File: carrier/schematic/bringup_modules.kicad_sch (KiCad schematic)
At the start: 56 parts, among them U301 SY6280AAC, U302 SY6280AAC, U303 SY6280AAC, U304 SY6280AAC, U305 SY6280AAC, U306 SY6280AAC, U307 SY6280AAC, U308 SY6280AAC

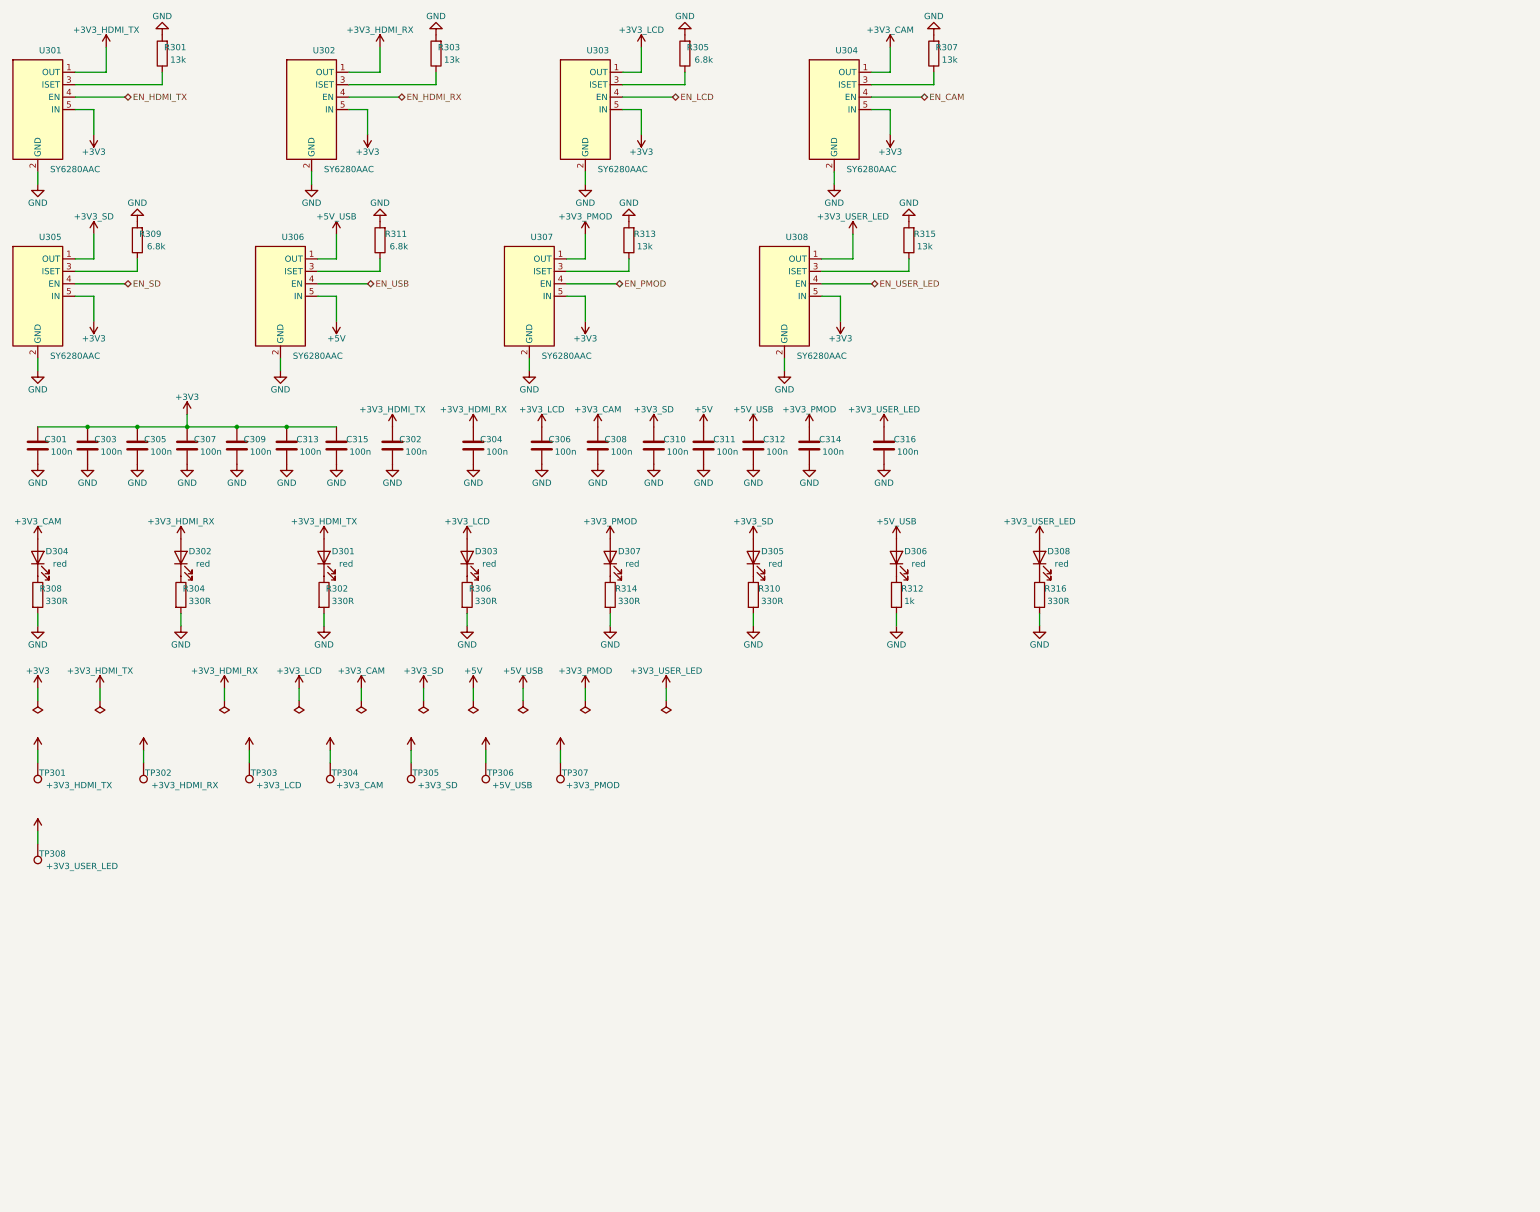
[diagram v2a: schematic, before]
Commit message: bringup: 5V MODULE GATES (PLAN round 5) — +5V_HDMI_TX/+5V_LCD SY6280 cells
Two new module gate cells resolve the power tree's last two UNSOURCED
findings, following the existing per-module pattern exactly:
- bringup_modules U9 +5V -> +5V_HDMI_TX (RSET 13k = 523 mA backstop; the
  load is TPD12S016-internally limited to 55 mA, DS 7.3.10) and U10
  +5V -> +5V_LCD (RSET 6.8k = 1.0 A for the 450 mA boost budget), 100n
  in/out, 1k status LEDs, TPs at the gated source.
- bringup_en_modules: 2 new SN74LVC1G08 AND cells (DIP master, SW veto).
- bringup_rails: SW1/SW2 positions were EXHAUSTED -> honest extension DIP
  SW6 (DSHP04TSGER, already-verified part; pos 1/2 wired, 3/4 author-NC
  spares) + TCA9535 P12/P13 vetos (P11 stays reserved for PMON_ALERT_N).
- bringup_facts.dip_switch_refs(): manual/firmware generators now discover
  every DSHP DIP instead of hard-coding SW1/SW2 — BRINGUP.md + the SC
  contract header regenerated with the new EN map automatically
  (ZC_TCA9535_BIT_EN_HDMI_TX_5V=10 / _EN_LCD_5V=11, SW6 stage-4 rows).
POWER TREE PASS: 14 regulators, findings 4->2, +5V buck at 91 % of 3 A.
All gates green (board exit 0); 3 drifted renders eyeballed full-res and
blessed; PWR_FLAG policy auto-stripped the now-driven rails' flags.

Co-Authored-By: Claude Fable 5 <noreply@anthropic.com>
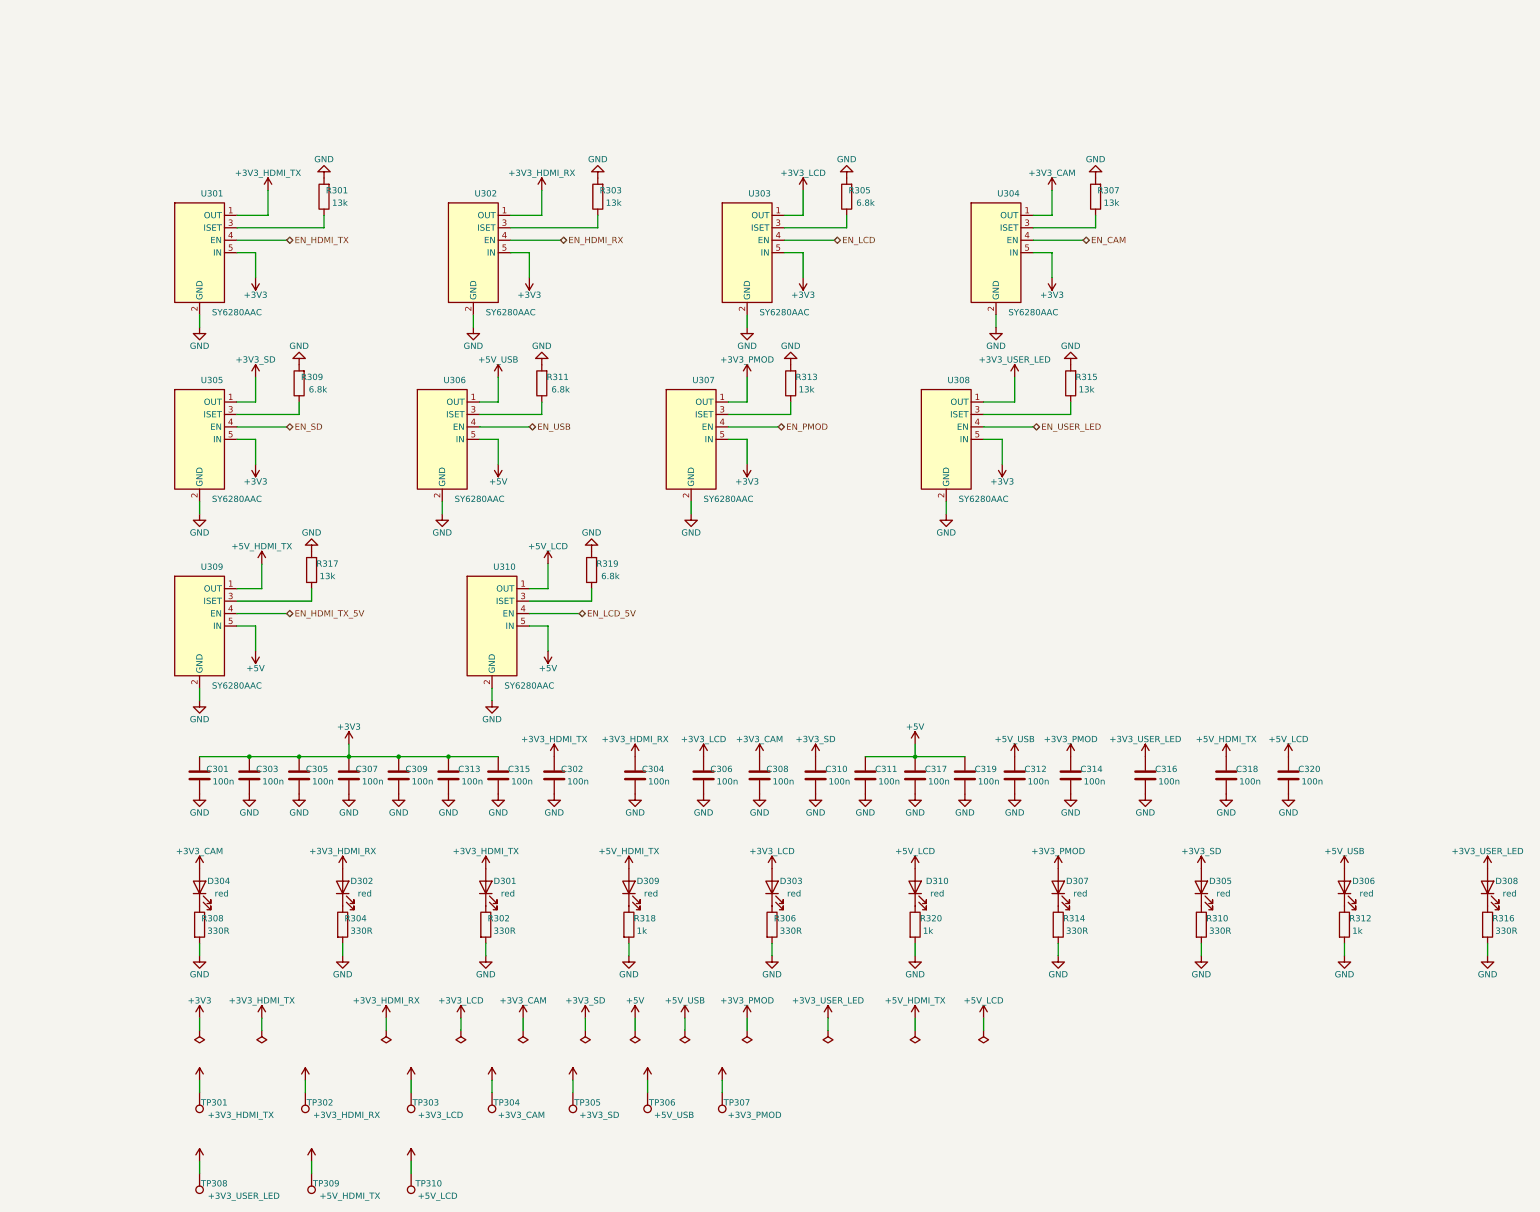
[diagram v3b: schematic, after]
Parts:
- added D306, D308: red, LED_SMD:LED_0603_1608Metric, symbol Device:LED
- added R312: 1k, Resistor_SMD:R_0603_1608Metric, symbol Device:R
- added R316: 330R, Resistor_SMD:R_0603_1608Metric, symbol Device:R
- added TP301: +3V3_HDMI_TX, TestPoint:TestPoint_Pad_D1.5mm, symbol Connector:TestPoint
- added TP302: +3V3_HDMI_RX, TestPoint:TestPoint_Pad_D1.5mm, symbol Connector:TestPoint
- added TP303: +3V3_LCD, TestPoint:TestPoint_Pad_D1.5mm, symbol Connector:TestPoint
- added TP304: +3V3_CAM, TestPoint:TestPoint_Pad_D1.5mm, symbol Connector:TestPoint
- added TP305: +3V3_SD, TestPoint:TestPoint_Pad_D1.5mm, symbol Connector:TestPoint
- added TP306: +5V_USB, TestPoint:TestPoint_Pad_D1.5mm, symbol Connector:TestPoint
- added TP307: +3V3_PMOD, TestPoint:TestPoint_Pad_D1.5mm, symbol Connector:TestPoint
- added TP308: +3V3_USER_LED, TestPoint:TestPoint_Pad_D1.5mm, symbol Connector:TestPoint
- added TP309: +5V_HDMI_TX, TestPoint:TestPoint_Pad_D1.5mm, symbol Connector:TestPoint
- added TP310: +5V_LCD, TestPoint:TestPoint_Pad_D1.5mm, symbol Connector:TestPoint
- C311: renamed from D304; value red -> 100n; footprint LED_SMD:LED_0603_1608Metric -> Capacitor_SMD:C_0603_1608Metric; symbol Device:LED -> Device:C; LCSC C2286 -> C1591
- C312: renamed from R304; value 330R -> 100n; footprint Resistor_SMD:R_0603_1608Metric -> Capacitor_SMD:C_0603_1608Metric; symbol Device:R -> Device:C; LCSC C23138 -> C1591
- C314: renamed from D301; value red -> 100n; footprint LED_SMD:LED_0603_1608Metric -> Capacitor_SMD:C_0603_1608Metric; symbol Device:LED -> Device:C; LCSC C2286 -> C1591
- C316: renamed from R302; value 330R -> 100n; footprint Resistor_SMD:R_0603_1608Metric -> Capacitor_SMD:C_0603_1608Metric; symbol Device:R -> Device:C; LCSC C23138 -> C1591
- C317: renamed from R308; value 330R -> 100n; footprint Resistor_SMD:R_0603_1608Metric -> Capacitor_SMD:C_0603_1608Metric; symbol Device:R -> Device:C; LCSC C23138 -> C1591
- C318: renamed from D303; value red -> 100n; footprint LED_SMD:LED_0603_1608Metric -> Capacitor_SMD:C_0603_1608Metric; symbol Device:LED -> Device:C; LCSC C2286 -> C1591
- C319: renamed from D302; value red -> 100n; footprint LED_SMD:LED_0603_1608Metric -> Capacitor_SMD:C_0603_1608Metric; symbol Device:LED -> Device:C; LCSC C2286 -> C1591
- C320: renamed from R306; value 330R -> 100n; footprint Resistor_SMD:R_0603_1608Metric -> Capacitor_SMD:C_0603_1608Metric; symbol Device:R -> Device:C; LCSC C23138 -> C1591
- D303: renamed from TP301; value +3V3_HDMI_TX -> red; footprint TestPoint:TestPoint_Pad_D1.5mm -> LED_SMD:LED_0603_1608Metric; symbol Connector:TestPoint -> Device:LED; BOM exclude -> (none); LCSC (none) -> C2286
- D305: renamed from TP307; value +3V3_PMOD -> red; footprint TestPoint:TestPoint_Pad_D1.5mm -> LED_SMD:LED_0603_1608Metric; symbol Connector:TestPoint -> Device:LED; BOM exclude -> (none); LCSC (none) -> C2286
- D307: renamed from TP305; value +3V3_SD -> red; footprint TestPoint:TestPoint_Pad_D1.5mm -> LED_SMD:LED_0603_1608Metric; symbol Connector:TestPoint -> Device:LED; BOM exclude -> (none); LCSC (none) -> C2286
- D310: renamed from TP303; value +3V3_LCD -> red; footprint TestPoint:TestPoint_Pad_D1.5mm -> LED_SMD:LED_0603_1608Metric; symbol Connector:TestPoint -> Device:LED; BOM exclude -> (none); LCSC (none) -> C2286
- R302: renamed from R312; value 1k -> 330R; LCSC C21190 -> C23138
- R306: renamed from TP302; value +3V3_HDMI_RX -> 330R; footprint TestPoint:TestPoint_Pad_D1.5mm -> Resistor_SMD:R_0603_1608Metric; symbol Connector:TestPoint -> Device:R; BOM exclude -> (none); LCSC (none) -> C23138
- R310: renamed from TP308; value +3V3_USER_LED -> 330R; footprint TestPoint:TestPoint_Pad_D1.5mm -> Resistor_SMD:R_0603_1608Metric; symbol Connector:TestPoint -> Device:R; BOM exclude -> (none); LCSC (none) -> C23138
- R314: renamed from TP306; value +5V_USB -> 330R; footprint TestPoint:TestPoint_Pad_D1.5mm -> Resistor_SMD:R_0603_1608Metric; symbol Connector:TestPoint -> Device:R; BOM exclude -> (none); LCSC (none) -> C23138
- R317: renamed from C303; value 100n -> 13k; footprint Capacitor_SMD:C_0603_1608Metric -> Resistor_SMD:R_0603_1608Metric; symbol Device:C -> Device:R; LCSC C1591 -> C22797
- R318: renamed from R316; value 330R -> 1k; LCSC C23138 -> C21190
- R319: renamed from C307; value 100n -> 6.8k; footprint Capacitor_SMD:C_0603_1608Metric -> Resistor_SMD:R_0603_1608Metric; symbol Device:C -> Device:R; LCSC C1591 -> C23212
- R320: renamed from TP304; value +3V3_CAM -> 1k; footprint TestPoint:TestPoint_Pad_D1.5mm -> Resistor_SMD:R_0603_1608Metric; symbol Connector:TestPoint -> Device:R; BOM exclude -> (none); LCSC (none) -> C21190
- U309: renamed from C301; value 100n -> SY6280AAC; footprint Capacitor_SMD:C_0603_1608Metric -> SY6280AAC:SY6280AAC; symbol Device:C -> SY6280AAC:SY6280AAC; LCSC C1591 -> C55136
- U310: renamed from C305; value 100n -> SY6280AAC; footprint Capacitor_SMD:C_0603_1608Metric -> SY6280AAC:SY6280AAC; symbol Device:C -> SY6280AAC:SY6280AAC; LCSC C1591 -> C55136
- renumbered C309 to C301, C310 to C302, C313 to C303, C311 to C304, C315 to C305, C312 to C306, C302 to C307, C314 to C308, C304 to C309, C316 to C310, C306 to C313, C308 to C315, D306 to D301, D305 to D302, D307 to D304, D308 to D309, R310 to R304, R314 to R308
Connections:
- net +3V3: now also C307.1, C309.1, C313.1, C315.1; no longer R317.1, R319.1, U309.1, U310.1
- net +3V3_CAM: now also C308.1, D304.2 (A), TP304.1; no longer C311.2 (A), C315.1, R320.1
- net +3V3_HDMI_RX: now also C304.1, D302.2 (A), TP302.1; no longer C309.1, C319.2 (A), R306.1
- net +3V3_HDMI_TX: now also C302.1, D301.2 (A), TP301.1; no longer C307.1, C314.2 (A), D303.1
- net +3V3_LCD: now also C306.1, D303.2 (A), TP303.1; no longer C313.1, C318.2 (A), D310.1
- net +3V3_PMOD: now also C314.1, D307.2 (A), TP307.1; no longer C308.1, D304.2 (A), D305.1
- net +3V3_SD: now also C310.1, D305.2 (A), TP305.1; no longer C302.1, D302.2 (A), D307.1
- net +3V3_USER_LED: now also C316.1, D308.2 (A), TP308.1; no longer C310.1, D309.2 (A), R310.1
- net +5V: now also C311.1, C317.1, C319.1, U309.5 (IN), U310.5 (IN); no longer C304.1
- net +5V_USB: now also C312.1, D306.2 (A), TP306.1; no longer C306.1, D301.2 (A), R314.1
- net GND: now also C311.2, C314.2, C318.2, C319.2, R306.2, R310.2, R314.2, R320.2, R312.2, R316.2
- net +5V_HDMI_TX: now reaches C318.1
- net +5V_HDMI_TX: now also D309.2 (A), U309.1 (OUT), TP309.1; no longer C320.1
- new net: R317.1, U309.3 (ISET)
- new net: D305.1 (K), R310.1
- new net: D306.1 (K), R312.1
- new net: D303.1 (K), R306.1
- new net: D310.1 (K), R320.1
- new net: D308.1 (K), R316.1
- new net: D307.1 (K), R314.1
- new net: R319.1, U310.3 (ISET)
- new net +5V_LCD: C320.1, D310.2 (A), TP310.1, U310.1 (OUT)
- new net EN_HDMI_TX_5V: U309.4 (EN)
- new net EN_LCD_5V: U310.4 (EN)
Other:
- moved on the sheet: C301, C302, C303, C304, C305, C306, C307, C308, C309, C310, C313, C315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

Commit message: audit-fix(engine): harvest F1-F7,F9 — gate hardening + leak + guards
F1 selftest now exercises the VISUAL gate against geometry mutants (wire-cross
+ text-over-wire) — proven to bite (was never run on a mutant before).
F2 visual_gate catches different-net wire T-touch / butt-join shorts.
F3 netlist_gate no longer leaks tmp .net files (was 2671 stale).
F4 board uniquify guards the stride (widened 100->1000) against ref collision.
F5 hier-mode sheets now re-run through the per-sheet netlist gate.
F6 dead clause dropped; F7 stale zynq_eda docstring fixed; F9 eager inline-pin
validation. Source copied verbatim from the audit-fix worktree (6 files, proven
untouched on origin since its base); board regenerated fresh. All gates green,
selftest geo-mutants killed by the visual gate, goldens 23/23, m1_rc PASS.

Co-Authored-By: Claude Fable 5 <noreply@anthropic.com>
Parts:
- renumbered C301 to C3001, C302 to C3002, C303 to C3003, C304 to C3004, C305 to C3005, C306 to C3006, C307 to C3007, C308 to C3008, C309 to C3009, C310 to C3010, C311 to C3011, C312 to C3012, C313 to C3013, C314 to C3014, C315 to C3015, C316 to C3016, C317 to C3017, C318 to C3018, C319 to C3019, C320 to C3020, D301 to D3001, D302 to D3002, D303 to D3003, D304 to D3004, D305 to D3005, D306 to D3006, D307 to D3007, D308 to D3008, D309 to D3009, D310 to D3010, R301 to R3001, R302 to R3002, R303 to R3003, R304 to R3004, R305 to R3005, R306 to R3006, R307 to R3007, R308 to R3008, R309 to R3009, R310 to R3010, R311 to R3011, R312 to R3012, R313 to R3013, R314 to R3014, R315 to R3015, R316 to R3016, R317 to R3017, R318 to R3018, R319 to R3019, R320 to R3020, TP301 to TP3001, TP302 to TP3002, TP303 to TP3003, TP304 to TP3004, TP305 to TP3005, TP306 to TP3006, TP307 to TP3007, TP308 to TP3008, TP309 to TP3009, TP310 to TP3010, U301 to U3001, U302 to U3002, U303 to U3003, U304 to U3004, U305 to U3005, U306 to U3006, U307 to U3007, U308 to U3008, U309 to U3009, U310 to U3010

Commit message: genpolish: TITLE-1 — populate the schematic title block on every sheet
Every sheet rendered a blank Title/Rev/Date — the clearest 'not a real
schematic' tell. emit() now writes a (title_block ...) after the paper node:
title = the sheet circuit's title, company "Zynq SoM Carrier", and a
"<sheet> — generated by schgen (do not hand-edit)" comment. NO date node — a
wall-clock date would break byte-determinism; the content-derived fields keep
every rebuild identical. Verified on A4 (usb_pd) and the dense A3 (power): the
block fills the standard reserved corner with zero drawing overlap. All 26
sheets, goldens re-blessed, board PASS + deterministic, selftest 53/53, m1,
pytest 147.

Co-Authored-By: Claude Opus 4.8 <noreply@anthropic.com>
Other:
- company: (none) -> Zynq SoM Carrier
- title: (none) -> Bring-up module gates: 10x SY6280 + status/user LEDs
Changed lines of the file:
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@@
 	(generator_version "1.0")
 	(paper "A3")
+	(title_block
+		(title "Bring-up module gates: 10x SY6280 + status/user LEDs")
+		(company "Zynq SoM Carrier")
+		(comment 1 "bringup_modules — generated by schgen (do not hand-edit)")
+	)
 	(wire
 		(pts

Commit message: board: four board-management HW blocks on a manually-gated +3V3_AUX (BOARDHW)
The four services the carrier was missing — all behind ONE manual power enable
(C1) on two new sheets split so neither defeats the placer's rail-stub router:

  board_aux       — the gate + I2C isolator (infrastructure)
  board_services  — ID-EEPROM + RTC + watchdog + QWIIC (the peripherals)

WHAT LANDED
  * 24AA025E48 (C129895)  ID-EEPROM with a factory EUI-48 **MAC** for the
      LAN8720/RJ45 — strapped 0x51 (0x50 is the FMC EEPROM).
  * RV-3028-C7 (C3019759) I2C RTC, integrated DTCXO (no crystal), CR1220 coin
      cell (KH-CR1220-2) with auto-switchover, 0x52.
  * TPS3823-33 (C7719)    supervisor + windowed watchdog.
  * ZX-SH1.0-4PWT (C7430446)  QWIIC / STEMMA-QT expansion (gated 3V3 + the
      isolated AUX I2C).
  * SY6280 gate + DSHP04 DIP + PCA9306 isolator complete the infrastructure.

CONSTRAINTS (the user's three standing requirements)
  C1 manual enable "like the previous": +3V3_AUX is a SY6280 load switch whose
     EN is a default-OFF DSHP04 DIP (100k pulldown) — the same gated-module
     idiom, self-contained so it touches none of the dense rail/EN sheets.
  C2 "no watchdog reset during power-up": THREE independent guards — (1) the
     supervisor's VDD is the default-OFF +3V3_AUX, so it is UNPOWERED through
     power-up; (2) the TPS3823 disables its watchdog while WDI floats, and WDI
     is driven only by the PL (WATCHDOG_KICK, Hi-Z until the fabric is up); (3)
     RESET# is a firmware-mediated PL EVENT (J3.31), never a rail/POR line.
  C3 Zynq-agnostic: the only SoM-side signals (the 2 watchdog lines) ride PL
     bank-35 IO by their contract net names (IO_L16_N/P_35 -> J3.29/31); xdc.py
     emits the constraints live — nothing hard-codes the Zynq part.

LAW 0 (electrical integrity): the peripherals sit on the GATED rail but their
bus is the always-on STM32_I2C2 management bus. A PCA9306 bridges them with EN
tied to +3V3_AUX, so the switch OPENS whenever the rail is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
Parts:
- renumbered C3001 to C5001, C3002 to C5002, C3003 to C5003, C3004 to C5004, C3005 to C5005, C3006 to C5006, C3007 to C5007, C3008 to C5008, C3009 to C5009, C3010 to C5010, C3011 to C5011, C3012 to C5012, C3013 to C5013, C3014 to C5014, C3015 to C5015, C3016 to C5016, C3017 to C5017, C3018 to C5018, C3019 to C5019, C3020 to C5020, D3001 to D5001, D3002 to D5002, D3003 to D5003, D3004 to D5004, D3005 to D5005, D3006 to D5006, D3007 to D5007, D3008 to D5008, D3009 to D5009, D3010 to D5010, R3001 to R5001, R3002 to R5002, R3003 to R5003, R3004 to R5004, R3005 to R5005, R3006 to R5006, R3007 to R5007, R3008 to R5008, R3009 to R5009, R3010 to R5010, R3011 to R5011, R3012 to R5012, R3013 to R5013, R3014 to R5014, R3015 to R5015, R3016 to R5016, R3017 to R5017, R3018 to R5018, R3019 to R5019, R3020 to R5020, TP3001 to TP5001, TP3002 to TP5002, TP3003 to TP5003, TP3004 to TP5004, TP3005 to TP5005, TP3006 to TP5006, TP3007 to TP5007, TP3008 to TP5008, TP3009 to TP5009, TP3010 to TP5010, U3001 to U5001, U3002 to U5002, U3003 to U5003, U3004 to U5004, U3005 to U5005, U3006 to U5006, U3007 to U5007, U3008 to U5008, U3009 to U5009, U3010 to U5010

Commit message: audit fixes: QWIIC ESD on its own sheet + firmware I2C-map completeness
Acting on a multi-agent adversarial re-audit of the 28-sheet board. Each
finding was independently re-verified before action — two confident "HIGH"
findings were FALSE POSITIVES whose proposed fixes would have INTRODUCED bugs,
and are documented-rejected, not applied:

  * "DSHP04 switches in parallel" — wrong. The footprint pads prove the pairing
    by physical opposition (switch n = pads n & 9-n): switch 1 = pads 1&8 is the
    only one on EN_AUX; the other even pins (2/4/6) are NC, identical to the
    proven bringup_rails SW6 idiom. The proposed "fix" (pins 1+2) wires two
    DIFFERENT switches and would leave EN_AUX permanently pulled down — the rail
    could never enable.
  * "PCA9306 EN floats when AUX is off" — wrong. A 100k to a 0 V rail pulls EN
    to 0 V (disabled), which is exactly TI's recommended "isolate when the gated
    side is unpowered" connection. No float.

REAL findings actioned:

1. QWIIC connector lacked ESD (every other external connector has it). Moved the
   QWIIC out of board_services onto its own sheet board_qwiic (the carrier's
   connectors-get-their-own-sheet idiom — rj45_connector, usb_uart_connector)
   and added a USBLC6-2SC6 low-cap ESD array at the connector (1<->6 / 3<->4
   passthrough, clamp ref +3V3_AUX). The dedicated sheet also keeps both sheets
   sparse enough for the rail-stub router. board_services drops to 9 parts.

2. schgen/firmware.py loaded only 7 sheets, so the SC-firmware contract + its
   I2C address-collision check were BLIND to the new devices. Added board_aux/
   board_services to SOURCES and three address rows: FMC-EEPROM 0x50, ID-EEPROM
   0x51 (DERIVED from the 24AA025E48 A1/A0 straps, so a mis-strap to 0x50 now
   trips the collision check against the FMC EEPROM), RTC 0x52. The firmware can
   now address the EUI-48 MAC EEPROM and the RTC. 114 -> 117 #defines.

3. board_services docstring clarified (EEPROM/RTC are on the PCA9306-i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
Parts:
- renumbered C5001 to C6001, C5002 to C6002, C5003 to C6003, C5004 to C6004, C5005 to C6005, C5006 to C6006, C5007 to C6007, C5008 to C6008, C5009 to C6009, C5010 to C6010, C5011 to C6011, C5012 to C6012, C5013 to C6013, C5014 to C6014, C5015 to C6015, C5016 to C6016, C5017 to C6017, C5018 to C6018, C5019 to C6019, C5020 to C6020, D5001 to D6001, D5002 to D6002, D5003 to D6003, D5004 to D6004, D5005 to D6005, D5006 to D6006, D5007 to D6007, D5008 to D6008, D5009 to D6009, D5010 to D6010, R5001 to R6001, R5002 to R6002, R5003 to R6003, R5004 to R6004, R5005 to R6005, R5006 to R6006, R5007 to R6007, R5008 to R6008, R5009 to R6009, R5010 to R6010, R5011 to R6011, R5012 to R6012, R5013 to R6013, R5014 to R6014, R5015 to R6015, R5016 to R6016, R5017 to R6017, R5018 to R6018, R5019 to R6019, R5020 to R6020, TP5001 to TP6001, TP5002 to TP6002, TP5003 to TP6003, TP5004 to TP6004, TP5005 to TP6005, TP5006 to TP6006, TP5007 to TP6007, TP5008 to TP6008, TP5009 to TP6009, TP5010 to TP6010, U5001 to U6001, U5002 to U6002, U5003 to U6003, U5004 to U6004, U5005 to U6005, U5006 to U6006, U5007 to U6007, U5008 to U6008, U5009 to U6009, U5010 to U6010
